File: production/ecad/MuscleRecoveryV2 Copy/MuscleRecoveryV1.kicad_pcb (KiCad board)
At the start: 2 copper layers, 122 parts, among them IC1 LC709203FQH-01TWG, J1 AudioJack3, J3 Motor_Screw_Terminal, J4 USB_C_Receptacle_USB2.0, J7 Conn_01x11_Pin, Q1 FDN340P, Q2 AO3400A, Q3 AO3400A, Q4 AO3400A, U1 AP1117-33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

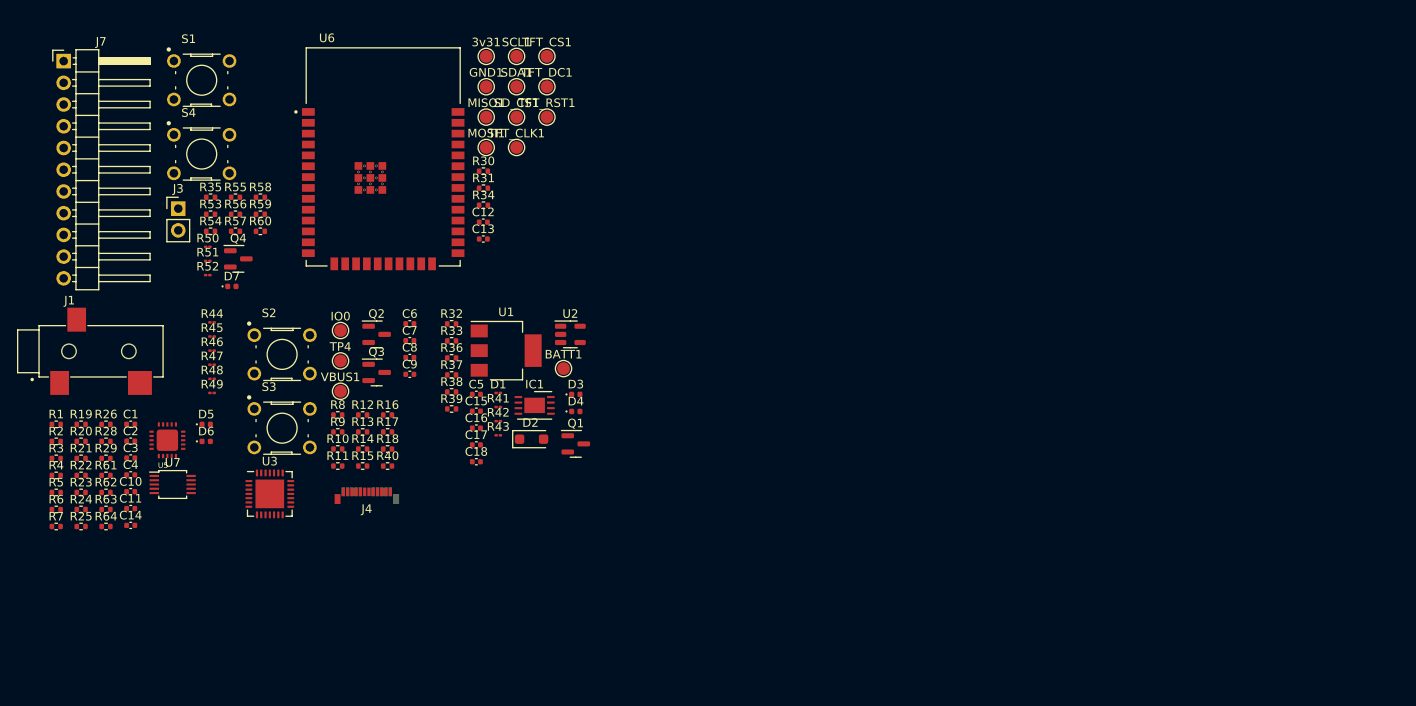
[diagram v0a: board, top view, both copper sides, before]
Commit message: Pushing Layout Changes for Andy's Layout
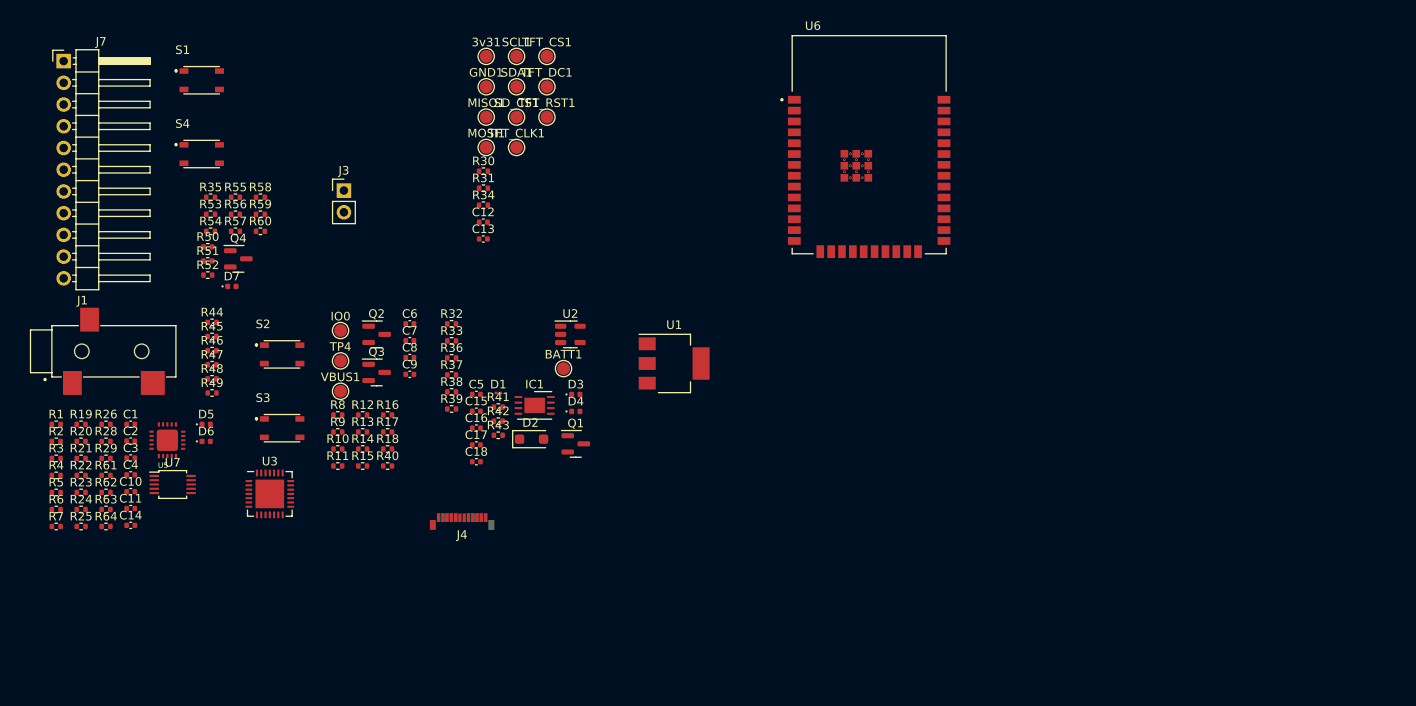
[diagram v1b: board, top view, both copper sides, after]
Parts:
- R41, R42, R43, R44, R45, R46, R47, R48, R49, R50, R51, R52: footprint Resistor_SMD:R_01005_0402Metric -> Resistor_SMD:R_0402_1005Metric
- S1, S2, S3, S4: footprint Muscle_Recovery_Footprint_Library:SW_B3F-1000 -> Muscle_Recovery_Footprint_Library:PTS810SJG250SMTRLFS
- moved U6 56.8 mm to (194.1, 50.0)
- moved U1 19.7 mm to (171.3, 75.5)
- moved J3 19.5 mm to (132.7, 55.3)
- moved J4 11.5 mm to (146.5, 93.5)
- moved J1 1.50 mm to (102.0, 74.1)

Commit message: Commiting More Muscle Recovery V2 Changes
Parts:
- added J2: Conn_01x02, Connector:JWT_A3963_1x02_P3.96mm_Vertical, F.Cu at (218.8, 51.0)
- moved C14 135.2 mm to (241.0, 71.9), turned to 90 degrees
- moved R29 133.6 mm to (237.1, 67.6)
- moved R62 131.7 mm to (234.7, 68.7)
- moved R61 131.5 mm to (234.7, 67.6), turned to 180 degrees
- moved U7 126.0 mm to (237.4, 71.2)
- moved R48 125.2 mm to (242.2, 69.5), turned to 90 degrees
- moved R47 123.9 mm to (241.0, 69.5), turned to 90 degrees
- moved R49 120.3 mm to (237.1, 68.7)
- moved Q1 94.7 mm to (254.4, 87.8), turned to -90 degrees
- moved U2 89.4 mm to (245.2, 96.4)
- moved C15 87.7 mm to (233.1, 103.0)
- moved C16 87.7 mm to (233.1, 105.0)
- moved C18 87.7 mm to (233.1, 108.9)
- moved C5 87.7 mm to (233.1, 101.1)
- moved D3 87.7 mm to (244.7, 101.1)
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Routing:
- net /Bootloading/RXD: track 0.00 -> 21.2 mm, vias 0 -> 2
- net /Bootloading/TXD: track 0.00 -> 19.9 mm, vias 0 -> 2
- net RTS: track 0.00 -> 17.2 mm, vias 0 -> 2
- net IO0: track 0.00 -> 8.38 mm
- net EN: track 0.00 -> 5.65 mm
- net DTR: track 0.00 -> 4.75 mm, vias 0 -> 1
- net GND: track 0.00 -> 4.74 mm, vias 0 -> 3
- net Net-(U7-SDA): track 0.00 -> 3.29 mm
- net Net-(U7-ALERT/RDY): track 0.00 -> 3.06 mm
- net /Bootloading/RTS_Q: track 0.00 -> 2.95 mm
- net Net-(U7-ADDR): track 0.00 -> 2.69 mm
- net /Bootloading/DTR_Q: track 0.00 -> 1.71 mm
- net Net-(U7-SCL): track 0.00 -> 1.64 mm
- net +3V3: track 0.00 -> 1.59 mm
- net ALERT/READY: track 0.00 -> 1.14 mm

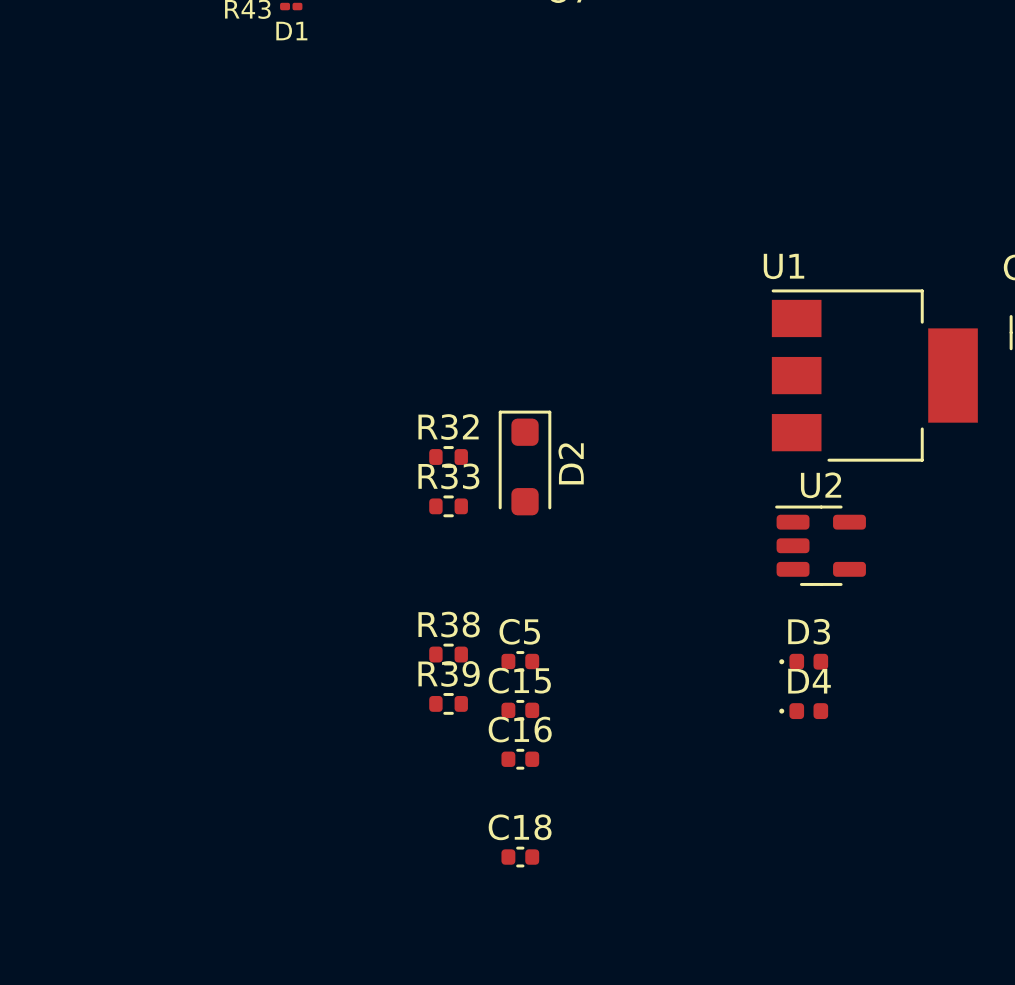
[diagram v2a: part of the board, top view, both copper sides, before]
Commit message: Adding routing with the EKG routing included
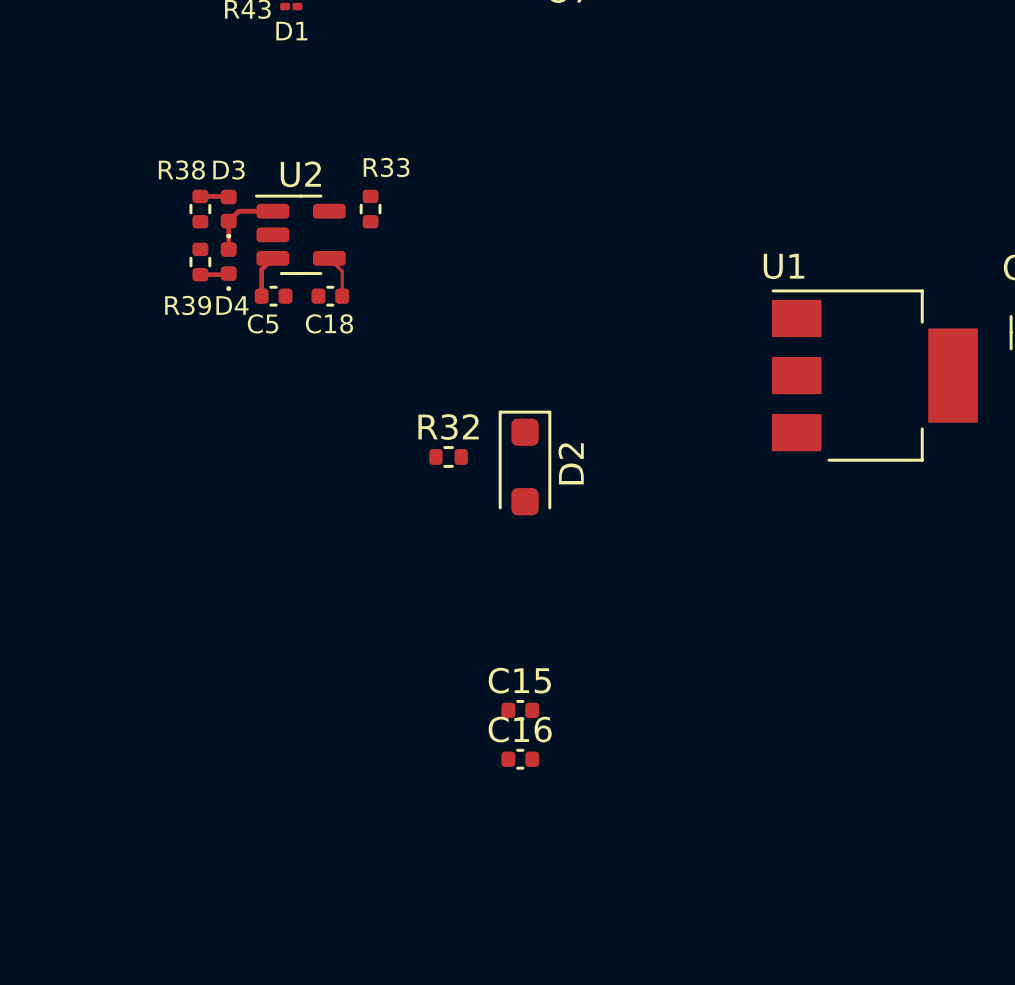
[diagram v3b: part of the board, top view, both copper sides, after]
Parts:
- moved D3 29.6 mm to (221.4, 82.8), turned to 90 degrees
- moved D4 29.6 mm to (221.4, 84.9), turned to 90 degrees
- moved U2 24.4 mm to (224.3, 83.9)
- moved C18 23.9 mm to (225.5, 86.3), turned to 180 degrees
- moved R38 20.5 mm to (220.2, 82.8), turned to 90 degrees
- moved R39 20.4 mm to (220.2, 85.0), turned to -90 degrees
- moved C5 17.8 mm to (223.2, 86.3)
- moved R33 12.4 mm to (227.1, 82.8), turned to -90 degrees
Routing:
- net Net-(D3-K): track 0.00 -> 3.09 mm
- net VBUS: track 0.00 -> 1.74 mm
- net +BATT: track 0.00 -> 1.71 mm
- net Net-(D4-K): track 0.00 -> 1.16 mm
- net Net-(D3-A): track 0.00 -> 1.15 mm

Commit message: Committing My pliminary placement for my PCB <3
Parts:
- removed 3v31, BATT1, GND1, IO0, MISO1, MOSI1, SCL1, SDA1, SD_CS1, TFT_CLK1, TFT_CS1, TFT_DC1, TFT_RST1, TP4, VBUS1: TestPoint, TestPoint:TestPoint_Pad_D1.5mm
- removed J1: AudioJack3, Muscle_Recovery_Footprint_Library:CUI_SJ-3523-SMT-TR
- removed R34, R35, R50, R51, R52, R53, R54, R55, R56: 0, Resistor_SMD:R_0402_1005Metric
- removed S4: B3F-1000, Muscle_Recovery_Footprint_Library:PTS810SJG250SMTRLFS
- added J5: SJ1-3533NG, Muscle_Recovery_Footprint_Library:CUI_SJ1-3533NG, F.Cu at (207.8, 107.8)
- added S5: TL1105VF160Q, Muscle_Recovery_Footprint_Library:SW_TL1105VF160Q, F.Cu at (172.2, 83.3)
- C12, C13, C15, C16: footprint Capacitor_SMD:C_0402_1005Metric -> Capacitor_SMD:C_0805_2012Metric
- J4: value USB_C_Receptacle_USB2.0 -> USB_C_Receptacle_HRO_TYPE-C-31-M-12; footprint Connector_USB:USB_C_Plug_Molex_105444 -> Connector_USB:USB_C_Receptacle_HRO_TYPE-C-31-M-12
- J7: value Conn_01x11_Pin -> 51296-1894; footprint Connector_PinHeader_2.54mm:PinHeader_1x11_P2.54mm_Horizontal -> Muscle_Recovery_Footprint_Library:512961894
- R32: footprint Resistor_SMD:R_0402_1005Metric -> Resistor_SMD:R_0805_2012Metric
- S1: value B3F-1000 -> TL1105VF160Q; footprint Muscle_Recovery_Footprint_Library:PTS810SJG250SMTRLFS -> Muscle_Recovery_Footprint_Library:SW_TL1105VF160Q
- moved J7 114.5 mm to (211.0, 68.2), turned to 180 degrees
- moved R7 114.1 mm to (212.8, 85.7)
- moved R6 114.1 mm to (212.8, 84.4), turned to 180 degrees
- moved R5 113.8 mm to (212.8, 88.1), turned to 180 degrees
- moved R24 111.4 mm to (212.8, 80.7)
- moved R23 110.3 mm to (212.2, 91.8), turned to 90 degrees
- moved R21 108.0 mm to (209.8, 91.8), turned to 90 degrees
- moved R22 106.7 mm to (208.7, 91.8), turned to 90 degrees
- moved R63 106.2 mm to (210.4, 81.0), turned to -90 degrees
- moved R19 105.9 mm to (207.5, 91.8), turned to 90 degrees
- moved R1 105.7 mm to (204.5, 90.2), turned to 180 degrees
- moved R3 105.6 mm to (204.5, 92.6)
- moved R2 105.5 mm to (204.5, 89.1), turned to 180 degrees
- moved R4 105.4 mm to (204.5, 87.9), turned to 180 degrees
- moved R64 105.3 mm to (209.3, 81.0), turned to 90 degrees
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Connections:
- J4 pad A1: GND -> (no net)
- J4 pad A12: GND -> (no net)
- J4 pad A4: VBUS -> (no net)
- J4 pad A5: Net-(J4-CC1) -> (no net)
- J4 pad A6: USB- -> (no net)
- J4 pad A7: USB+ -> (no net)
- J4 pad A8: unconnected-(J4-SBU1-PadA8) -> (no net)
- J4 pad A9: VBUS -> (no net)
- J4 pad B1: GND -> (no net)
- J4 pad B12: GND -> (no net)
- J4 pad B4: VBUS -> (no net)
- J4 pad B5: Net-(J4-CC2) -> (no net)
- J4 pad B8: unconnected-(J4-SBU2-PadB8) -> (no net)
- J4 pad B9: VBUS -> (no net)
- J4 pad S1: unconnected-(J4-SHIELD-PadS1) -> (no net)
- J7 pad 1: unconnected-(J7-Pin_1-Pad1) -> +3.3V
- J7 pad 10: Net-(J7-Pin_10) -> LIT
- J7 pad 11: Net-(J7-Pin_11) -> unconnected-(J7-Pad11)
- J7 pad 2: +3.3V -> GND
- J7 pad 3: GND -> SCK
- J7 pad 4: Net-(J7-Pin_4) -> MISO
- J7 pad 5: Net-(J7-Pin_5) -> MOSI
- J7 pad 6: Net-(J7-Pin_6) -> TFT_CS
- J7 pad 7: Net-(J7-Pin_7) -> TFT_RST
- J7 pad 8: Net-(J7-Pin_8) -> TFT_DC
- J7 pad 9: Net-(J7-Pin_9) -> SD_CS
- S1 pad 1: unconnected-(S1-Pad1) -> ALT_START_BUTTON
- S1 pad 2: START_BUTTON -> +3.3V
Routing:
- net MOTOR_EN: track 0.00 -> 29.3 mm, vias 0 -> 2
- net TXD0: track 0.00 -> 28.5 mm
- net RXD0: track 0.00 -> 27.1 mm
- net Vout: track 0.00 -> 24.0 mm, vias 0 -> 3
- net IO0: track 8.38 -> 28.7 mm, vias 0 -> 2
- net START_BUTTON: track 0.00 -> 15.1 mm
- net ALT_START_BUTTON: track 0.00 -> 13.4 mm
- net EN: track 5.65 -> 15.3 mm
- net Net-(U5-FR): track 0.00 -> 8.83 mm, vias 0 -> 2
- net REF: track 0.00 -> 8.02 mm
- net SDA: track 0.00 -> 7.82 mm
- net Net-(U5-RLD): track 0.00 -> 6.51 mm
- net SW: track 0.00 -> 6.30 mm, vias 0 -> 2
- net Net-(U5-HPSENSE): track 0.00 -> 6.10 mm
- net TFT_CS: track 0.00 -> 5.12 mm, vias 0 -> 1
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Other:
- board outline added: 50.7 x 55.6 mm
- board text added: "J7"

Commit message: Adding STEP file
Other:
- board text added: "BOOT"
- board text added: "EKG IN"
- board text added: "RST"
- board text added: "TO SCREEN"
- board text added: "USER BTN"
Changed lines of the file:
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@@
     (pad "29" smd rect (at 0 0) (size 3.35 3.35) (layers "F.Cu" "F.Mask")
       (net 10 "GND") (pinfunction "GND") (pintype "passive"))
-    (model "${KICAD6_3DMODEL_DIR}/Package_DFN_QFN.3dshapes/QFN-28-1EP_5x5mm_P0.5mm_EP3.35x3.35mm.wrl"
+    (model "${KICAD7_3DMODEL_DIR}/Package_DFN_QFN.3dshapes/QFN-28-1EP_5x5mm_P0.5mm_EP3.35x3.35mm.step"
       (offset (xyz 0 0 0))
       (scale (xyz 1 1 1))
@@
     (property "SnapEDA_Link" "https://www.snapeda.com/parts/B3F-1000/Omron+Electronics+Inc-EMC+Div/view-part/?ref=snap")
     (attr smd)
-    (fp_text reference "S2" (at -3.81 -0.83 180) (layer "F.SilkS")
+    (fp_text reference "S2" (at -0.123 0.0762 180) (layer "F.SilkS")
         (effects (font (size 0.75 0.75) (thickness 0.15)))
     )
@@
     (pad "2" thru_hole oval (at 0 2.54 180) (size 1.7 1.7) (drill 1) (layers "*.Cu" "*.Mask")
       (net 26 "Net-(D7-A)") (pinfunction "Pin_2") (pintype "passive"))
-    (model "${KICAD6_3DMODEL_DIR}/Connector_PinHeader_2.54mm.3dshapes/PinHeader_1x02_P2.54mm_Vertical.wrl"
+    (model "${KICAD7_3DMODEL_DIR}/Connector_PinHeader_2.54mm.3dshapes/PinHeader_1x02_P2.54mm_Vertical.step"
       (offset (xyz 0 0 0))
       (scale (xyz 1 1 1))
@@
     (pad "3" smd roundrect (at 0.9375 0) (size 1.475 0.6) (layers "F.Cu" "F.Paste" "F.Mask") (roundrect_rratio 0.25)
       (net 10 "GND") (pinfunction "D") (pintype "passive"))
-    (model "${KICAD6_3DMODEL_DIR}/Package_TO_SOT_SMD.3dshapes/SOT-23.wrl"
+    (model "${KICAD7_3DMODEL_DIR}/Package_TO_SOT_SMD.3dshapes/SOT-23.step"
       (offset (xyz 0 0 0))
       (scale (xyz 1 1 1))
@@
     (property "ki_keywords" "battery charger lithium")
     (attr smd)
-    (fp_text reference "U2" (at 2.921 1.0668 180) (layer "F.SilkS")
+    (fp_text reference "U2" (at 2.921 1.0668) (layer "F.SilkS")
         (effects (font (size 0.75 0.75) (thickness 0.15)))
     )
@@
     (pad "5" smd roundrect (at 1.1375 -0.95 270) (size 1.325 0.6) (layers "F.Cu" "F.Paste" "F.Mask") (roundrect_rratio 0.25)
       (net 72 "Net-(U2-PROG)") (pinfunction "PROG") (pintype "input"))
-    (model "${KICAD6_3DMODEL_DIR}/Package_TO_SOT_SMD.3dshapes/SOT-23-5.wrl"
+    (model "${KICAD7_3DMODEL_DIR}/Package_TO_SOT_SMD.3dshapes/SOT-23-5.step"
       (offset (xyz 0 0 0))
       (scale (xyz 1 1 1))
@@
     (property "ki_keywords" "Battery gauge I2C")
     (attr smd)
-    (fp_text reference "IC1" (at -3.175 2.413 -180) (layer "F.SilkS")
+    (fp_text reference "IC1" (at -3.175 2.413) (layer "F.SilkS")
         (effects (font (size 0.75 0.75) (thickness 0.15)))
     )
@@
     (pad "9" smd rect (at 0 0 270) (size 2.4 1.8) (layers "F.Cu" "F.Mask")
       (net 10 "GND") (pinfunction "EP") (pintype "passive"))
-    (model "${KICAD6_3DMODEL_DIR}/Package_DFN_QFN.3dshapes/WDFN-8-1EP_4x3mm_P0.65mm_EP2.4x1.8mm.wrl"
+    (model "${KICAD7_3DMODEL_DIR}/Package_DFN_QFN.3dshapes/WDFN-8-1EP_4x3mm_P0.65mm_EP2.4x1.8mm.step"
       (offset (xyz 0 0 0))
       (scale (xyz 1 1 1))
@@
     (pad "S1" thru_hole oval (at 4.32 -3.13) (size 1 2.1) (drill oval 0.6 1.7) (layers "*.Cu" "*.Mask"))
     (pad "S1" thru_hole oval (at 4.32 1.05) (size 1 1.6) (drill oval 0.6 1.2) (layers "*.Cu" "*.Mask"))
-    (model "${KICAD6_3DMODEL_DIR}/Connector_USB.3dshapes/USB_C_Receptacle_HRO_TYPE-C-31-M-12.wrl"
+    (model "${KICAD7_3DMODEL_DIR}/Connector_USB.3dshapes/USB_C_Receptacle_GCT_USB4105-xx-A_16P_TopMnt_Horizontal.step"
       (offset (xyz 0 0 0))
       (scale (xyz 1 1 1))
       (rotate (xyz 0 0 0))
     )
-    (model ":KICAD7_3DMODEL_DIR:Connector_USB.3dshapes/USB_C_Receptacle_GCT_USB4105-xx-A_16P_TopMnt_Horizontal.wrl"
+    (model "${KICAD7_3DMODEL_DIR}/Connector_USB.3dshapes/USB_C_Receptacle_GCT_USB4105-xx-A_16P_TopMnt_Horizontal.step" hide
       (offset (xyz 0 0 0))
       (scale (xyz 1 1 1))
@@
     (property "Sheetname" "Display")
     (attr through_hole)
-    (fp_text reference "S1" (at -5.024 1.564 -180) (layer "F.SilkS")
+    (fp_text reference "S1" (at -0.056 -0.087 -180) (layer "F.SilkS")
         (effects (font (size 1.4 1.4) (thickness 0.15)))
     )
@@
     (pad "10" smd rect (at 2.15 -1) (size 1.1 0.25) (layers "F.Cu" "F.Paste" "F.Mask")
       (net 76 "Net-(U7-SCL)") (pinfunction "SCL") (pintype "input"))
-    (model "${KICAD6_3DMODEL_DIR}/Package_SO.3dshapes/TSSOP-10_3x3mm_P0.5mm.wrl"
+    (model "${KICAD7_3DMODEL_DIR}/Package_SO.3dshapes/TSSOP-10_3x3mm_P0.5mm.step"
       (offset (xyz 0 0 0))
       (scale (xyz 1 1 1))
@@
     (property "SnapEDA_Link" "https://www.snapeda.com/parts/B3F-1000/Omron+Electronics+Inc-EMC+Div/view-part/?ref=snap")
     (attr smd)
-    (fp_text reference "S3" (at -3.683 0 180) (layer "F.SilkS")
+    (fp_text reference "S3" (at -0.254 0.0762 180) (layer "F.SilkS")
         (effects (font (size 0.75 0.75) (thickness 0.15)))
     )
@@
     (property "ki_keywords" "connector")
     (attr through_hole)
-    (fp_text reference "J2" (at -3.232 4.191 -180) (layer "F.SilkS")
+    (fp_text reference "J2" (at -3.232 4.191) (layer "F.SilkS")
         (effects (font (size 1 1) (thickness 0.15)))
     )
@@
     (pad "2" thru_hole circle (at 3.88 0 270) (size 3 3) (drill 1.75) (layers "*.Cu" "*.Mask")
       (net 10 "GND") (pinfunction "Pin_2") (pintype "passive"))
-    (model "${KICAD6_3DMODEL_DIR}/Connector.3dshapes/JWT_A3963_1x02_P3.96mm_Vertical.wrl"
+    (model "${KICAD6_3DMODEL_DIR}/Connector.3dshapes/JWT_A3963_1x02_P3.96mm_Vertical.wrl" hide
       (offset (xyz 0 0 0))
       (scale (xyz 1 1 1))
       (rotate (xyz 0 0 0))
     )
+    (model ":KICAD7_3DMODEL_DIR:Connector_PinSocket_2.54mm.3dshapes/PinSocket_1x02_P2.54mm_Vertical.step" hide
+      (offset (xyz 0.5 0 0))
+      (scale (xyz 1 1 1))
+      (rotate (xyz 0 0 -90))
+    )
+    (model "C:/Users/aabre/Desktop/kicad/Kicad External Parts/CHECKED/282834-2.step"
+      (offset (xyz 2 -0.5 0))
+      (scale (xyz 1.5 1.1 1.2))
+      (rotate (xyz -90 0 0))
+    )
   )
   (footprint "Capacitor_SMD:C_0402_1005Metric" (layer "F.Cu")
@@
   (gr_line (start 219.268918 107.696) (end 219.268918 63.627)
     (stroke (width 0.1) (type default)) (layer "Edge.Cuts"))
+  (gr_text "RST" (at 197.866 111.76) (layer "F.SilkS" knockout)
+    (effects (font (size 1 1) (thickness 0.15)) (justify left bottom))
+  )
+  (gr_text "USER\nBTN\n" (at 169.418 68.453) (layer "F.SilkS" knockout)
+    (effects (font (size 1 1) (thickness 0.15)) (justify left bottom))
+  )
+  (gr_text "BOOT\n" (at 192.151 111.76) (layer "F.SilkS" knockout)
+    (effects (font (size 1 1) (thickness 0.15)) (justify left bottom))
+  )
+  (gr_text "EKG\nIN\n" (at 210.693 112.903) (layer "F.SilkS" knockout)
+    (effects (font (size 1 1) (thickness 0.15)) (justify left bottom))
+  )
   (gr_text "J7" (at 204.47 64.262) (layer "F.SilkS")
     (effects (font (size 1 1) (thickness 0.15)))
   )
+  (gr_text "TO SCREEN" (at 209.042 73.279) (layer "F.SilkS" knockout)
+    (effects (font (size 1 1) (thickness 0.15)) (justify left bottom))
+  )
   (dimension (type aligned) (layer "Edge.Cuts")
